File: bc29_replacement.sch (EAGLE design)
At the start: 4 parts, among them IC1 ATMEGA328P, IC17 CD4070B, J2 2520-5

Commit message: MCU and PCB dimensions
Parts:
- removed IC1: ATMEGA328P, adafruit:ATMEGA168-20P
- added C12: .47uF, rcl:C-EUC0805
- added C13: 10uF, rcl:C-EUC0805
- added C15: 2.2nF, rcl:C-EUC0805
- added C27: 0.1u, SparkFun-Capacitors:CAP-0805
- added C9: .1uF, rcl:C-EUC0805
- added D1: BAT54, diode:BAT54
- added JP1: JTAG, pinhead:PINHD-2X7
- added R10: 20.0K, rcl:R-EU_R0805
- added R27: 0R0, rcl:R-EU_R0805
- added R36: 300, rcl:R-EU_R0805
- added R9: 47K, rcl:R-EU_R0805
- added S2: SPST-PTH-6.0MM, SparkFun-Switches:MOMENTARY-SWITCH-SPST-PTH-6.0MM
- added U9: MSP430I2041TPW, TI_MSP430_v16:MSP430I204XTPW
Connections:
- new net A0.0+: U9.1
- new net A0.0-: U9.2
- new net A1.0+: U9.3
- new net A1.0-: U9.4
- new net A2.0+: U9.5
- new net A2.0-: U9.6
- new net A3.0+: U9.7
- new net A3.0-: U9.8
- new net AGND: C27.2, R10.2, R27.2, U9.10
- new net P1.0: U9.17
- new net P1.1: U9.18
- new net P1.4: U9.21
- new net P1.5: U9.22
- new net P1.6: U9.23
- new net P1.7: U9.24
- new net P2.0: U9.25
- new net P2.1: U9.26
- new net P2.2: U9.27
- new net P2.3: U9.28
- new net ROSC: R10.1, U9.11
- new net RST_JTAG: C15.2, JP1.1, R36.1, R9.1, U9.15
- new net RST_PB: R36.2, S2.2
- new net SBWTCK: JP1.7, U9.16
- new net UCA0RXD: JP1.14, U9.19
- new net UCA0TXD: JP1.12, U9.20
- new net VCC: C13.2, C9.1, D1.C, R9.2, U9.13
- new net VCC_JTAG: D1.A, JP1.2
- new net VCORE: C12.2, U9.14
- new net VREF: C27.1, U9.9
- net GND: now also C12.1, C13.1, C15.1, C9.2, JP1.9, R27.1, S2.1, U9.12
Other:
- note added: "From .../docs/DS_msp430i2040.pdf, Table 5-21: SD24 has max differential input of +-928mV @ gain = 1 to maintain spec. SD24 has max common mode input of VCC to -1V. Each SD24 input has 200K input impedence to AVSS."
- note added: "MCU & REF"

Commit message: input network
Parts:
- added C1: 100nF, rcl:C-EUC1206
- added C19, C21: 10nF, rcl:C-EUC0805
- added C2: 33uF 450V, rcl:CPOL-EUE7.5-18
- added C3, C4, C5: 47pF, rcl:C-EUC0805
- added D2: P6KEXXC, diode:P6KEXXC
- added D8: 1N4448, diode:DIODE-MINIMELF
- added D9: 1N4004, diode:DIODE-SOD80C
- added E2: 10uF 63V, rcl:CPOL-EUE2.5-5
- added E3: 47uf 25V, rcl:CPOL-EUE2.5-5
- added F1: 32mA, fuse:FUSEBLANK_5X20MM
- added IC18: LP2951, linear:LP2951D
- added L1: 8mH, inductor-neosid:Z14/40CCW
- added L2, L3: (no value), inductor-neosid:SM-B9
- added M1: IRF740, transistor-power:IRF740
- added R2, R3: 1.0K, rcl:R-EU_R0805
- added R29, R30: 1M, rcl:R-EU_M0805
- added X1: 236-412, con-wago-508:236-412
- added Z1: 12V, diode:ZENER-DIODESOD80C
- added Z2: 6.2V, diode:ZENER-DIODESOD80C
- J2: value 2520-5 -> 2520-; device con-3m:2520-5 -> con-3m:2520-
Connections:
- new net !NAR: X1-5.KL1
- new net !RESET: X1-7.KL1
- new net +BATT: F1.1, L1.1, X1-1.KL1
- new net +BATT_FILT: C2.+, L1.2
- new net 12+: X1-11.KL1
- new net 12-: X1-12.KL1
- new net 13V5: D8.A, E2.+, IC18.IN, M1.S
- new net AH_NEGATIVE: X1-8.KL1
- new net DRAIN: D9.C, M1.D
- new net FUSED_BATT+: D9.A, F1.2, R30.2
- new net GATE: C21.1, D8.C, M1.G, R29.2, Z1.C
- new net GND1K: X1-6.KL1
- new net N$1: D2.2, L2.1
- new net N$2: D2.1, L3.1
- new net N$29: R29.1, R30.1
- new net N$44: IC18.FB, IC18.VOTAB
- new net N$5: L2.2, R2.2
- new net N$8: L3.2, R3.2
- new net OUT+: X1-9.KL1
- new net OUT-: X1-10.KL1
- new net SHUNT+: X1-4.KL1
- new net SHUNT-: X1-3.KL1
- net +5V: now also C1.1, C19.1, E3.+, IC18.OUT, IC18.SENSE, Z1.A, Z2.C
- net A0.0+: now also C4.1, C5.1, R3.1
- net A0.0-: now also C3.2, C5.2, R2.1
- net GND: now also C1.2, C19.2, C2.-, C21.2, C3.1, C4.2, E2.-, E3.-, IC18.GND, X1-2.KL1, Z2.A
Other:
- note added: "13.5VDC"
- note added: "Positive Voltage Regulator"

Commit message: io expansion
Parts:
- added IC1: 74HCS596D, 74xx-us:74LS596D
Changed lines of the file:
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@@
 <setting verticaltext="up"/>
 </settings>
-<grid distance="0.1" unitdist="inch" unit="inch" style="lines" multiple="1" display="yes" altdistance="0.01" altunitdist="inch" altunit="inch"/>
+<grid distance="0.1" unitdist="inch" unit="inch" style="lines" multiple="1" display="no" altdistance="0.01" altunitdist="inch" altunit="inch"/>
 <layers>
 <layer number="1" name="Top" color="4" fill="1" visible="no" active="no"/>
@@
 <part name="C4" library="rcl" deviceset="C-EU" device="C0805" value="47pF"/>
 <part name="C5" library="rcl" deviceset="C-EU" device="C0805" value="47pF"/>
+<part name="IC1" library="74xx-us" deviceset="74*596" device="D" technology="LS" value="74HCS596D"/>
 </parts>
 <sheets>
@@
 <instance part="SUPPLY3" gate="+5V" x="363.22" y="-10.16" rot="R90"/>
 <instance part="R1" gate="G$1" x="373.38" y="-10.16"/>
+<instance part="IC1" gate="A" x="195.58" y="22.86"/>
 </instances>
 <busses>

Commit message: power
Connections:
- net +BATT: no longer F1.1
- net +BATT_FILT: now also F1.1
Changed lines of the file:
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@@
 <text x="63.5" y="63.5" size="1.778" layer="91">13.5VDC</text>
 <text x="63.5" y="63.5" size="1.778" layer="91">13.5VDC</text>
-<text x="58.42" y="68.58" size="5.08" layer="91">Positive Voltage Regulator</text>
+<text x="45.72" y="86.36" size="5.08" layer="91">Positive Voltage Regulator</text>
 </plain>
 <instances>
@@
 </busses>
 <nets>
-<net name="+BATT" class="0">
-<segment>
-<pinref part="F1" gate="G$1" pin="1"/>
-<wire x1="0" y1="60.96" x2="17.78" y2="60.96" width="0.1524" layer="91"/>
-</segment>
-</net>
 <net name="GND" class="0">
 <segment>
@@
 </segment>
 </net>
+<net name="+BATT_FILT" class="0">
+<segment>
+<pinref part="F1" gate="G$1" pin="1"/>
+<wire x1="0" y1="60.96" x2="17.78" y2="60.96" width="0.1524" layer="91"/>
+</segment>
+</net>

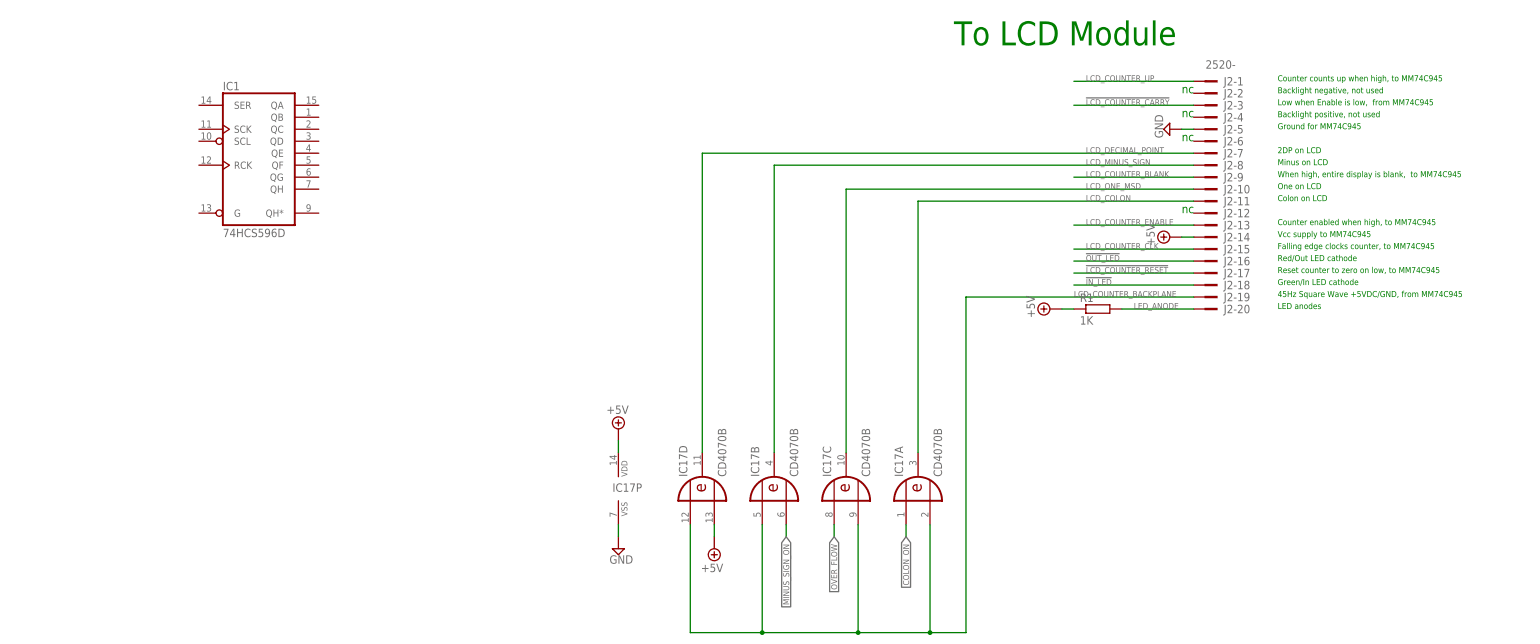
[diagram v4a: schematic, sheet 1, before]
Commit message: add shift register
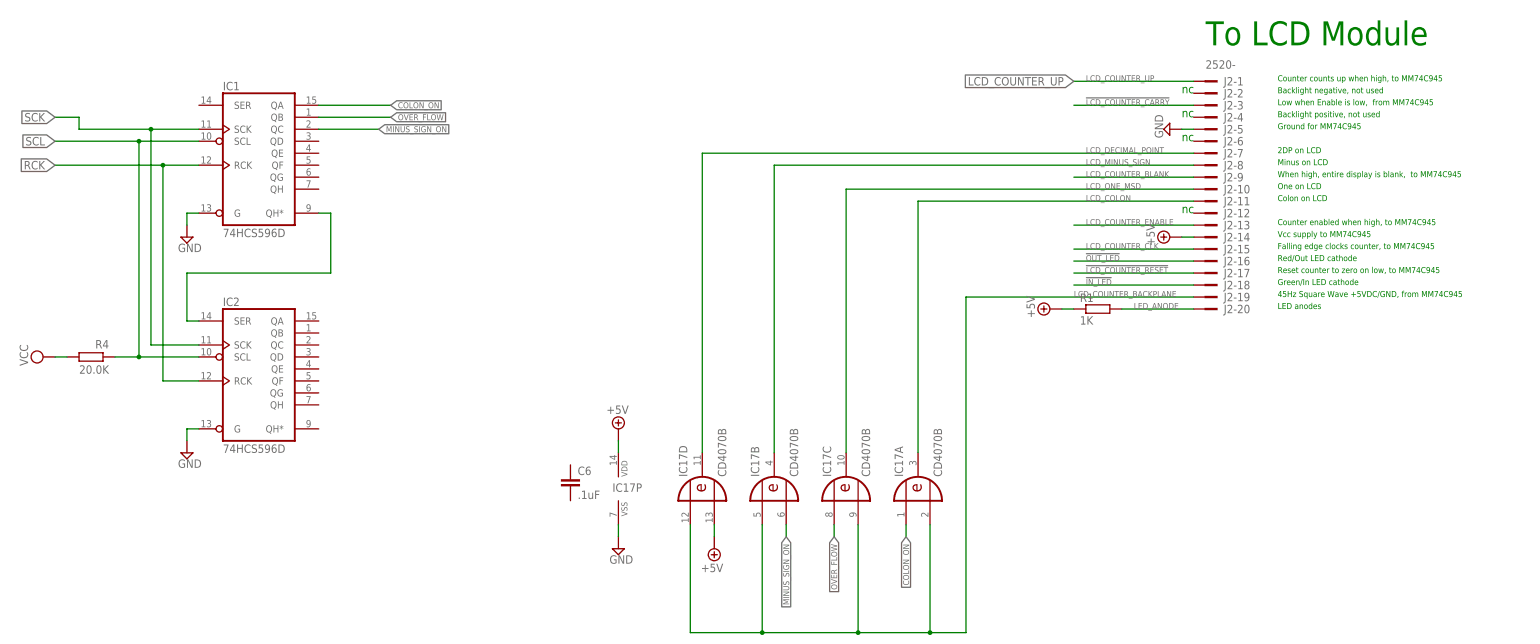
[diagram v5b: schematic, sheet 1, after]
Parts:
- added C6: .1uF, rcl:C-EUC0805
- added IC2: 74HCS596D, 74xx-us:74LS596D
- added R4: 20.0K, rcl:R-EU_R0805
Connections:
- new net N$4: IC1A.QH*, IC2A.SER
- new net RCK: IC1A.RCK, IC2A.RCK
- new net SCK: IC1A.SCK, IC2A.SCK
- new net SCL: IC1A.SCL, IC2A.SCL, R4.1
- net GND: now also IC1A.G, IC2A.G
- net VCC: now also R4.2
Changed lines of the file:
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@@
 <setting verticaltext="up"/>
 </settings>
-<grid distance="0.1" unitdist="inch" unit="inch" style="lines" multiple="1" display="no" altdistance="0.01" altunitdist="inch" altunit="inch"/>
+<grid distance="0.1" unitdist="inch" unit="inch" style="lines" multiple="1" display="yes" altdistance="0.01" altunitdist="inch" altunit="inch"/>
 <layers>
 <layer number="1" name="Top" color="4" fill="1" visible="no" active="no"/>
@@
 <part name="C5" library="rcl" deviceset="C-EU" device="C0805" value="47pF"/>
 <part name="IC1" library="74xx-us" deviceset="74*596" device="D" technology="LS" value="74HCS596D"/>
+<part name="IC2" library="74xx-us" deviceset="74*596" device="D" technology="LS" value="74HCS596D"/>
+<part name="SUPPLY13" library="supply2" deviceset="GND" device=""/>
+<part name="SUPPLY14" library="supply2" deviceset="GND" device=""/>
+<part name="C6" library="rcl" deviceset="C-EU" device="C0805" value=".1uF"/>
+<part name="SUPPLY15" library="supply2" deviceset="VCC" device=""/>
+<part name="R4" library="rcl" deviceset="R-EU_" device="R0805" value="20.0K "/>
 </parts>
 <sheets>
 <sheet>
 <plain>
-<text x="342.9" y="45.72" size="5.08" layer="91">To LCD Module</text>
+<text x="396.24" y="45.72" size="5.08" layer="91">To LCD Module</text>
 <text x="391.16" y="10.16" size="1.778" layer="91">nc</text>
 <text x="391.16" y="25.4" size="1.778" layer="91">nc</text>
@@
 <instance part="R1" gate="G$1" x="373.38" y="-10.16"/>
 <instance part="IC1" gate="A" x="195.58" y="22.86"/>
+<instance part="IC2" gate="A" x="195.58" y="-22.86"/>
+<instance part="SUPPLY13" gate="GND" x="180.34" y="5.08"/>
+<instance part="SUPPLY14" gate="GND" x="180.34" y="-40.64"/>
+<instance part="C6" gate="G$1" x="261.62" y="-45.72" smashed="yes">
+<attribute name="NAME" x="263.144" y="-45.339" size="1.778" layer="95"/>
+<attribute name="VALUE" x="263.144" y="-50.419" size="1.778" layer="96"/>
+</instance>
+<instance part="SUPPLY15" gate="G$1" x="149.86" y="-20.32" smashed="yes" rot="R90">
+<attribute name="VALUE" x="146.685" y="-22.225" size="1.778" layer="96" rot="R90"/>
+</instance>
+<instance part="R4" gate="G$1" x="160.02" y="-20.32" smashed="yes" rot="R180">
+<attribute name="NAME" x="163.83" y="-16.7386" size="1.778" layer="95" rot="R180"/>
+<attribute name="VALUE" x="163.83" y="-22.098" size="1.778" layer="96" rot="R180"/>
+</instance>
 </instances>
 <busses>
@@
 <wire x1="271.78" y1="-58.42" x2="271.78" y2="-55.88" width="0.1524" layer="91"/>
 </segment>
+<segment>
+<pinref part="IC1" gate="A" pin="G"/>
+<wire x1="182.88" y1="10.16" x2="180.34" y2="10.16" width="0.1524" layer="91"/>
+<pinref part="SUPPLY13" gate="GND" pin="GND"/>
+<wire x1="180.34" y1="10.16" x2="180.34" y2="7.62" width="0.1524" layer="91"/>
+</segment>
+<segment>
+<pinref part="IC2" gate="A" pin="G"/>
+<wire x1="182.88" y1="-35.56" x2="180.34" y2="-35.56" width="0.1524" layer="91"/>
+<pinref part="SUPPLY14" gate="GND" pin="GND"/>
+<wire x1="180.34" y1="-35.56" x2="180.34" y2="-38.1" width="0.1524" layer="91"/>
+</segment>
 </net>
 <net name="+5V" class="0">
@@
 <label x="317.5" y="-58.42" size="1.27" layer="95" rot="R270" xref="yes"/>
 </segment>
+<segment>
+<wire x1="208.28" y1="30.48" x2="223.52" y2="30.48" width="0.1524" layer="91"/>
+<label x="223.52" y="30.48" size="1.27" layer="95" xref="yes"/>
+</segment>
 </net>
 <net name="MINUS_SIGN_ON" class="0">
@@
 <label x="307.34" y="-58.42" size="1.27" layer="95" rot="R270" xref="yes"/>
 </segment>
+<segment>
+<wire x1="208.28" y1="27.94" x2="220.98" y2="27.94" width="0.1524" layer="91"/>
+<label x="220.98" y="27.94" size="1.27" layer="95" xref="yes"/>
+</segment>
 </net>
 <net name="COLON_ON" class="0">
@@
 <wire x1="332.74" y1="-55.88" x2="332.74" y2="-58.42" width="0.1524" layer="91"/>
 <label x="332.74" y="-58.42" size="1.27" layer="95" rot="R270" xref="yes"/>
+</segment>
+<segment>
+<wire x1="208.28" y1="33.02" x2="223.52" y2="33.02" width="0.1524" layer="91"/>
+<label x="223.52" y="33.02" size="1.27" layer="95" xref="yes"/>
 </segment>
 </net>
@@
 <wire x1="393.7" y1="38.1" x2="368.3" y2="38.1" width="0.1524" layer="91"/>
 <label x="370.84" y="38.1" size="1.27" layer="95"/>
+<label x="368.3" y="38.1" size="1.778" layer="95" rot="R180" xref="yes"/>
 </segment>
 </net>
@@
 </segment>
 </net>
+<net name="N$4" class="0">
+<segment>
+<pinref part="IC1" gate="A" pin="QH*"/>
+<wire x1="210.82" y1="10.16" x2="208.28" y2="10.16" width="0.1524" layer="91"/>
+<wire x1="210.82" y1="-2.54" x2="180.34" y2="-2.54" width="0.1524" layer="91"/>
+<wire x1="180.34" y1="-2.54" x2="180.34" y2="-12.7" width="0.1524" layer="91"/>
+<pinref part="IC2" gate="A" pin="SER"/>
+<wire x1="180.34" y1="-12.7" x2="182.88" y2="-12.7" width="0.1524" layer="91"/>
+<wire x1="210.82" y1="10.16" x2="210.82" y2="-2.54" width="0.1524" layer="91"/>
+</segment>
+</net>
+<net name="SCK" class="0">
+<segment>
+<pinref part="IC1" gate="A" pin="SCK"/>
+<wire x1="182.88" y1="27.94" x2="172.72" y2="27.94" width="0.1524" layer="91"/>
+<pinref part="IC2" gate="A" pin="SCK"/>
+<wire x1="182.88" y1="-17.78" x2="172.72" y2="-17.78" width="0.1524" layer="91"/>
+<wire x1="172.72" y1="-17.78" x2="172.72" y2="27.94" width="0.1524" layer="91"/>
+<wire x1="172.72" y1="27.94" x2="157.48" y2="27.94" width="0.1524" layer="91"/>
+<wire x1="157.48" y1="27.94" x2="157.48" y2="30.48" width="0.1524" layer="91"/>
+<wire x1="157.48" y1="30.48" x2="152.4" y2="30.48" width="0.1524" layer="91"/>
+<label x="152.4" y="30.48" size="1.778" layer="95" rot="R180" xref="yes"/>
+<junction x="172.72" y="27.94"/>
+</segment>
+</net>
+<net name="SCL" class="0">
+<segment>
+<pinref part="IC2" gate="A" pin="SCL"/>
+<pinref part="R4" gate="G$1" pin="1"/>
+<wire x1="165.1" y1="-20.32" x2="170.18" y2="-20.32" width="0.1524" layer="91"/>
+<pinref part="IC1" gate="A" pin="SCL"/>
+<wire x1="170.18" y1="-20.32" x2="182.88" y2="-20.32" width="0.1524" layer="91"/>
+<wire x1="182.88" y1="25.4" x2="170.18" y2="25.4" width="0.1524" layer="91"/>
+<wire x1="170.18" y1="25.4" x2="170.18" y2="-20.32" width="0.1524" layer="91"/>
+<junction x="170.18" y="-20.32"/>
+<wire x1="170.18" y1="25.4" x2="152.4" y2="25.4" width="0.1524" layer="91"/>
+<label x="152.4" y="25.4" size="1.778" layer="95" rot="R180" xref="yes"/>
+<junction x="170.18" y="25.4"/>
+</segment>
+</net>
+<net name="VCC" class="0">
+<segment>
+<pinref part="SUPPLY15" gate="G$1" pin="VCC"/>
+<pinref part="R4" gate="G$1" pin="2"/>
+<wire x1="154.94" y1="-20.32" x2="152.4" y2="-20.32" width="0.1524" layer="91"/>
+</segment>
+</net>
+<net name="RCK" class="0">
+<segment>
+<pinref part="IC1" gate="A" pin="RCK"/>
+<wire x1="182.88" y1="20.32" x2="175.26" y2="20.32" width="0.1524" layer="91"/>
+<wire x1="175.26" y1="20.32" x2="175.26" y2="-25.4" width="0.1524" layer="91"/>
+<pinref part="IC2" gate="A" pin="RCK"/>
+<wire x1="175.26" y1="-25.4" x2="182.88" y2="-25.4" width="0.1524" layer="91"/>
+<wire x1="175.26" y1="20.32" x2="152.4" y2="20.32" width="0.1524" layer="91"/>
+<label x="152.4" y="20.32" size="1.778" layer="95" rot="R180" xref="yes"/>
+<junction x="175.26" y="20.32"/>
+</segment>
+</net>
